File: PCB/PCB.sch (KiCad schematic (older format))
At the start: 120 parts, among them J2 USB-C USB 2.0 MC-372, J3 Conn_01x04, J4 Conn_01x02, Q1 AO3407, Q2 AO3406, SW1 MSK-12C02, U1 E73-2G4M08S1C, U2 MCP73831, U3 AP2112K-3.3

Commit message: Complete matrix
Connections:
- wire segments 165 -> 183
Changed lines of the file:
@@
 Text Label 6500 1450 1    50   ~ 0
 P1.11
+Text Label 7000 1450 1    50   ~ 0
+P0.03
+Text Label 7500 1450 1    50   ~ 0
+P0.28
+Text Label 8000 1450 1    50   ~ 0
+P1.13
+Text Label 8500 1450 1    50   ~ 0
+P0.02
+Text Label 9000 1450 1    50   ~ 0
+P0.29
+Text Label 9500 1450 1    50   ~ 0
+P0.31
+Text Label 10000 1450 1    50   ~ 0
+P0.30
+Text Label 10500 1450 1    50   ~ 0
+P0.00
+Text Label 11000 1450 1    50   ~ 0
+P0.01
+Text Label 11500 1450 1    50   ~ 0
+P0.05
+Text Label 12000 1450 1    50   ~ 0
+P0.12
+Text Label 12500 1450 1    50   ~ 0
+P0.10
+Text Label 13000 1450 1    50   ~ 0
+P0.09
+Text Label 13500 1700 0    50   ~ 0
+P1.04
+Text Label 13000 2200 0    50   ~ 0
+P1.00
+Text Label 13000 2700 0    50   ~ 0
+P0.24
+Text Label 11500 3200 0    50   ~ 0
+P0.22
+Wire Wire Line
+	11500 3200 11400 3200
+Connection ~ 11400 3200
+Wire Wire Line
+	13000 2700 12900 2700
+Connection ~ 12900 2700
+Wire Wire Line
+	13000 2200 12900 2200
+Connection ~ 12900 2200
+Wire Wire Line
+	13500 1700 13400 1700
+Connection ~ 13400 1700
+Wire Wire Line
+	13000 1450 13000 1500
+Wire Wire Line
+	12500 1450 12500 1500
+Connection ~ 12500 1500
+Wire Wire Line
+	12000 1450 12000 1500
+Connection ~ 12000 1500
+Wire Wire Line
+	11500 1450 11500 1500
+Connection ~ 11500 1500
+Wire Wire Line
+	11000 1450 11000 1500
+Connection ~ 11000 1500
+Wire Wire Line
+	10500 1450 10500 1500
+Connection ~ 10500 1500
+Wire Wire Line
+	10000 1450 10000 1500
+Connection ~ 10000 1500
+Wire Wire Line
+	9500 1450 9500 1500
+Connection ~ 9500 1500
+Wire Wire Line
+	9000 1450 9000 1500
+Connection ~ 9000 1500
+Wire Wire Line
+	8500 1450 8500 1500
+Connection ~ 8500 1500
+Wire Wire Line
+	8000 1450 8000 1500
+Connection ~ 8000 1500
+Wire Wire Line
+	7500 1450 7500 1500
+Connection ~ 7500 1500
+Wire Wire Line
+	7000 1450 7000 1500
+Connection ~ 7000 1500
+Wire Wire Line
+	6500 1450 6500 1500
+Connection ~ 6500 1500
 $EndSCHEMATC

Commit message: Add reset button
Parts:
- added SW? (x2): SW_Push, symbol Switch:SW_Push
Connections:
- wire segments 183 -> 185
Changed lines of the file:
@@
 Connection ~ 9000 2500
 Wire Wire Line
-	9000 2500 9000 3000
+	9000 2500 9000 2920
 Wire Wire Line
 	9500 1500 9500 2000
@@
 	6500 1450 6500 1500
 Connection ~ 6500 1500
+$Comp
+L Switch:SW_Push SW?
+U 1 1 5EC49318
+P 9200 2920
+F 0 "SW?" H 9200 3095 50  0000 C CNN
+F 1 "SW_Push" H 9200 3114 50  0001 C CNN
+F 2 "" H 9200 3120 50  0001 C CNN
+F 3 "~" H 9200 3120 50  0001 C CNN
+	1    9200 2920
+	1    0    0    -1
+$EndComp
+Connection ~ 9000 2920
+Wire Wire Line
+	9000 2920 9000 3000
+Wire Wire Line
+	9400 2920 9400 3000
+Connection ~ 9400 3000
+$Comp
+L Switch:SW_Push SW?
+U 1 1 5EC53F12
+P 4680 5135
+F 0 "SW?" H 4680 5420 50  0000 C CNN
+F 1 "SW_Push" H 4680 5329 50  0000 C CNN
+F 2 "" H 4680 5335 50  0001 C CNN
+F 3 "~" H 4680 5335 50  0001 C CNN
+	1    4680 5135
+	1    0    0    -1
+$EndComp
+$Comp
+L power:GND #PWR?
+U 1 1 5EC56230
+P 4880 5135
+F 0 "#PWR?" H 4880 4885 50  0001 C CNN
+F 1 "GND" V 4880 5015 50  0000 R CNN
+F 2 "" H 4880 5135 50  0001 C CNN
+F 3 "" H 4880 5135 50  0001 C CNN
+	1    4880 5135
+	0    -1   -1   0
+$EndComp
+Text GLabel 4480 5135 0    50   Input ~ 0
+RESET
 $EndSCHEMATC

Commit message: Sort scheme
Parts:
- J2: footprint nrfmicro:HRO-TYPE-C-31-M-12 -> HRO-TYPE-C-31-M-12
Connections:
- no-connect marks 7 -> 5
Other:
- note added: "USB Scheme\n"
- moved on the sheet: C2, D2, D3, D?, J3, J4, Q2, R2, R4, R5, R6, R7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

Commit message: Clear all annotation
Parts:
- renumbered C3 to C?, C2 to C?, C1 to C?, D1 to D?, D3 to D?, D2 to D?, J2 to J?, J3 to J?, J4 to J?, Q1 to Q?, Q2 to Q?, R3 to R?, R2 to R?, R5 to R?, R4 to R?, R7 to R?, R6 to R?, R8 to R?, R1 to R?, R9 to R?, SW1 to SW?, U1 to U?, U2 to U?, U3 to U?

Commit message: Anotate components
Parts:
- gave numbers to parts that had none: 122

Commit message: Start PCB work
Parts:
- C2, C3: symbol nrfmicro-rescue:C -> PCB-rescue:C-nrfmicro-rescue
- D1, D10, D11, D12, D13, D14, D15, D16, D17, D18, D19, D2, D20, D21, D22, D23, D24, D25, D26, D27, D28, D29, D3, D30, D31, D32, D33, D34, D35, D36, D37, D38, D39, D4, D40, D41, D42, D43, D44, D45, D46, D47, D48, D5, D6, D7, D8, D9: footprint (none) -> Used_Footprints:Diode_SMD_SOD-123
- D51: symbol nrfmicro-rescue:MBR0520 -> PCB-rescue:MBR0520-nrfmicro-rescue
- J1: footprint HRO-TYPE-C-31-M-12 -> Type-C:HRO-TYPE-C-31-M-12; symbol nrfmicro:HRO-TYPE-C-31-M-12 -> PCB-rescue:HRO-TYPE-C-31-M-12-nrfmicro
- J3: footprint nrfmicro:connector_bat -> nrfmicro:connector_swd
- Q1: symbol nrfmicro-rescue:BSS83P -> PCB-rescue:BSS83P-nrfmicro-rescue
- R6, R8, R9: symbol nrfmicro-rescue:R -> PCB-rescue:R-nrfmicro-rescue
- SW1, SW10, SW11, SW12, SW13, SW14, SW16, SW17, SW18, SW19, SW2, SW20, SW21, SW22, SW23, SW24, SW25, SW26, SW29, SW3, SW30, SW31, SW32, SW33, SW34, SW35, SW36, SW37, SW38, SW4, SW40, SW42, SW44, SW47, SW49, SW5, SW6, SW7, SW8, SW9: footprint (none) -> Infinity:SW_MxHotswap_1u
- SW15, SW39, SW43, SW48: footprint (none) -> Infinity:SW_MxHotswap_1.25u
- SW27, SW28: footprint (none) -> Infinity:SW_MxHotswap_1.75u
- SW41: footprint (none) -> Infinity:SW_MxHotswap_7u
- SW45: footprint (none) -> Infinity:SW_MxHotswap_2.25u
- SW46: footprint (none) -> Infinity:SW_MxHotswap_2.75u
- SW50: footprint (none) -> Keebio-Parts:SW_SPST_TL3342
- U1: symbol nrfmicro:E73-2G4M08S1C-52840 -> PCB-rescue:E73-2G4M08S1C-52840-nrfmicro

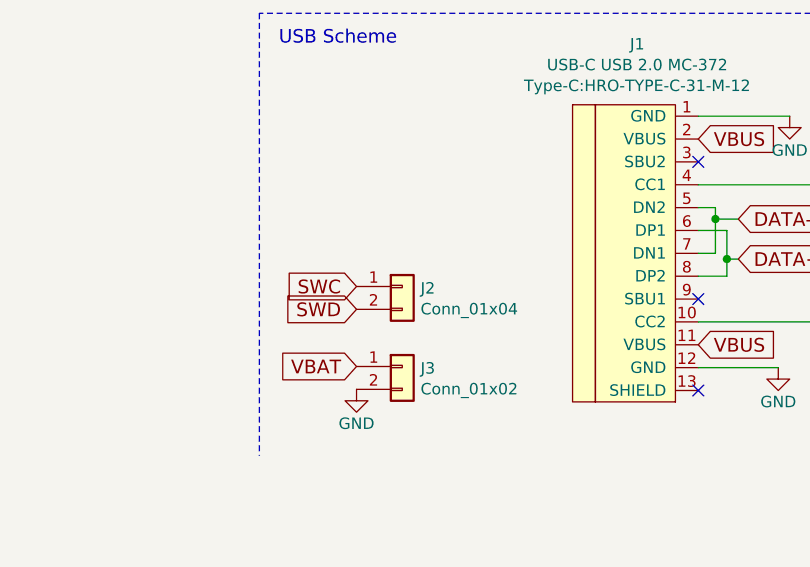
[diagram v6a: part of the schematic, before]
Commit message: Remove useless silkscreen
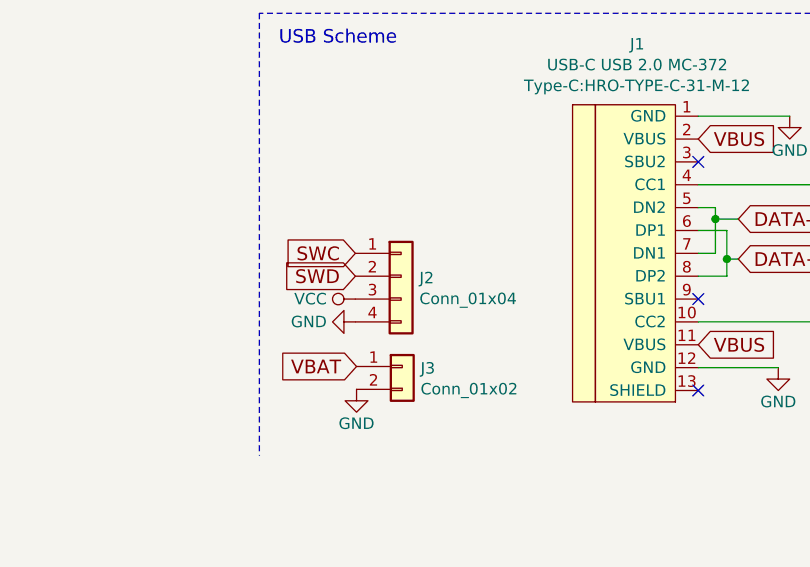
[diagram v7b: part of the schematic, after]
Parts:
- removed J2: Conn_01x04, nrfmicro:connector_swd, symbol Connector_Generic:Conn_01x02
- added J2: Conn_01x04, nrfmicro:connector_swd, symbol Connector_Generic:Conn_01x04
- J3: footprint nrfmicro:connector_swd -> nrfmicro:connectro_bat
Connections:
- net GND: now also J2.4 (Pin_4)
- net SWC: now also J2.1 (Pin_1)
- net SWD: now also J2.2 (Pin_2)
- net VCC: now also J2.3 (Pin_3)
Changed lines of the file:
@@
 Text GLabel 3300 1550 2    60   Input ~ 0
 SWC
-Text GLabel 8730 5795 0    60   Input ~ 0
+Text GLabel 8725 5650 0    60   Input ~ 0
 SWC
-Text GLabel 8730 5895 0    60   Input ~ 0
+Text GLabel 8725 5750 0    60   Input ~ 0
 SWD
 $Comp
@@
 $EndComp
 $Comp
-L Connector_Generic:Conn_01x02 J2
-U 1 1 5CDF605B
-P 8930 5795
-F 0 "J2" H 9010 5787 50  0000 L CNN
-F 1 "Conn_01x04" H 9010 5696 50  0000 L CNN
-F 2 "nrfmicro:connector_swd" H 8930 5795 50  0001 C CNN
-F 3 "~" H 8930 5795 50  0001 C CNN
-	1    8930 5795
-	1    0    0    -1
-$EndComp
-$Comp
 L Connector_Generic:Conn_01x02 J3
 U 1 1 5DA92B59
@@
 F 0 "J3" H 9010 6137 50  0000 L CNN
 F 1 "Conn_01x02" H 9010 6046 50  0000 L CNN
-F 2 "nrfmicro:connector_swd" H 8930 6145 50  0001 C CNN
+F 2 "nrfmicro:connectro_bat" H 8930 6145 50  0001 C CNN
 F 3 "~" H 8930 6145 50  0001 C CNN
 	1    8930 6145
@@
 Text Notes 8390 4745 0    59   ~ 0
 USB Scheme\n
+$Comp
+L Connector_Generic:Conn_01x04 J2
+U 1 1 5ED6D234
+P 8925 5750
+F 0 "J2" H 9005 5742 50  0000 L CNN
+F 1 "Conn_01x04" H 9005 5651 50  0000 L CNN
+F 2 "nrfmicro:connector_swd" H 8925 5750 50  0001 C CNN
+F 3 "~" H 8925 5750 50  0001 C CNN
+	1    8925 5750
+	1    0    0    -1
+$EndComp
+$Comp
+L power:VCC #PWR0101
+U 1 1 5ED75EB4
+P 8725 5850
+F 0 "#PWR0101" H 8725 5700 50  0001 C CNN
+F 1 "VCC" V 8725 5975 50  0000 L CNN
+F 2 "" H 8725 5850 50  0001 C CNN
+F 3 "" H 8725 5850 50  0001 C CNN
+	1    8725 5850
+	0    -1   -1   0
+$EndComp
+$Comp
+L power:GND #PWR0102
+U 1 1 5ED79AA3
+P 8725 5950
+F 0 "#PWR0102" H 8725 5700 50  0001 C CNN
+F 1 "GND" V 8725 5825 50  0000 R CNN
+F 2 "" H 8725 5950 50  0001 C CNN
+F 3 "" H 8725 5950 50  0001 C CNN
+	1    8725 5950
+	0    1    1    0
+$EndComp
 $EndSCHEMATC
